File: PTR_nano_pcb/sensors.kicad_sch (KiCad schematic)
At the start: 9 parts, among them U2 LSM6DSO32, U3 BMP280

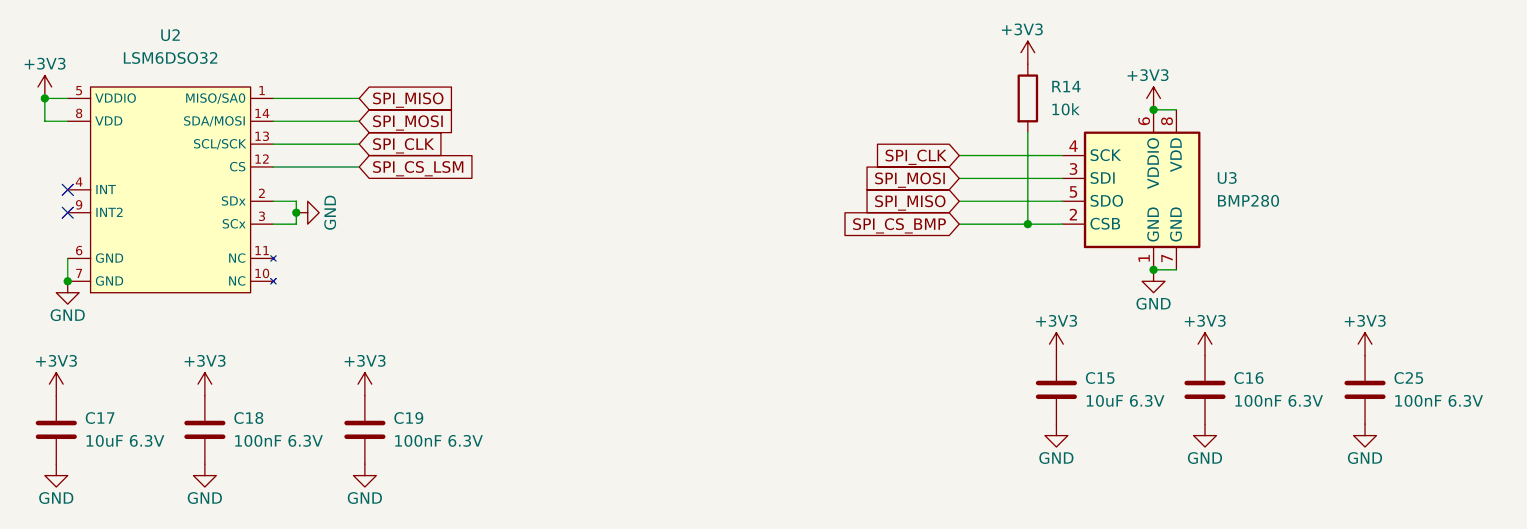
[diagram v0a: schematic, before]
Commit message: Pressure sensor changed to BMP581
+ library fixed
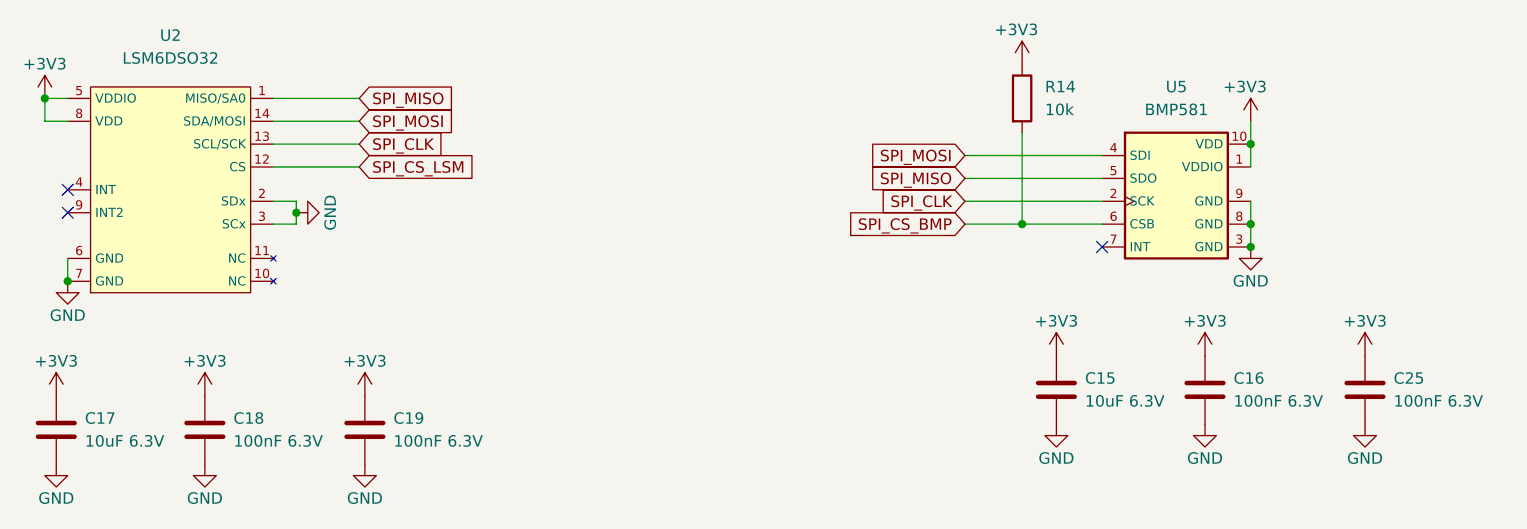
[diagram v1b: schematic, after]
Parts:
- removed U3: BMP280, Package_LGA:Bosch_LGA-8_2x2.5mm_P0.65mm_ClockwisePinNumbering, symbol Sensor_Pressure:BMP280
- added U5: BMP581, PTR_nano_footprint:BMP581, symbol ptr_nano_lib:BMP581
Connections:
- net +3V3: now also U5.1 (VDDIO), U5.10 (VDD)
- net GND: now also U5.3 (GND), U5.8 (GND), U5.9 (GND)
- net SPI_CLK: now also U5.2 (SCK)
- net SPI_CS_BMP: now also U5.6 (CSB)
- net SPI_MISO: now also U5.5 (SDO)
- net SPI_MOSI: now also U5.4 (SDI)
- no-connect marks 2 -> 3
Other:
- moved on the sheet: R14
